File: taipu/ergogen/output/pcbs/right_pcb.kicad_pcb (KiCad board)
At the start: 2 copper layers, 162.9 x 92.4 mm, 0 parts

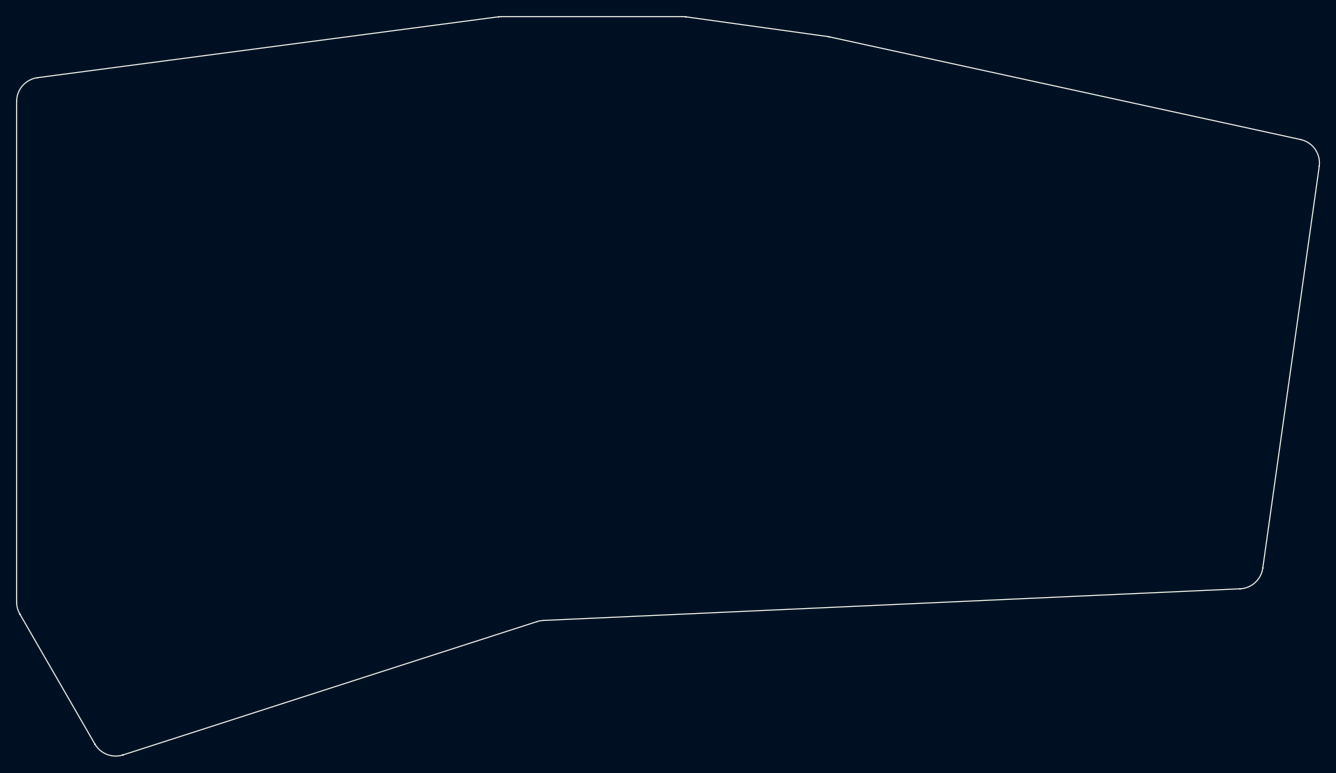
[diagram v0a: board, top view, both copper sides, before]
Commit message: mounting holes and net
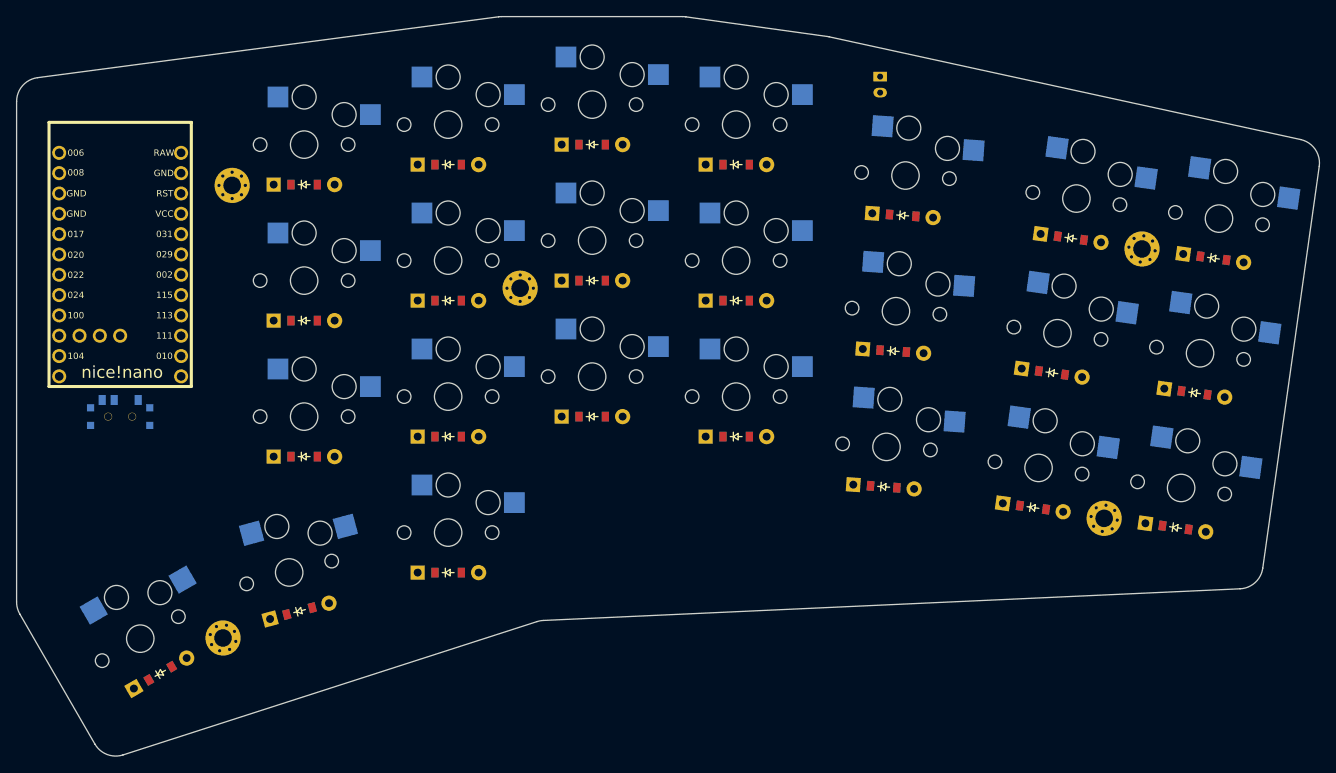
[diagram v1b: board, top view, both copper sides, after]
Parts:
- added D1: , ComboDiode, F.Cu at (376.2, 138.1)
- added D10: , ComboDiode, F.Cu at (321.3, 126.7)
- added D11: , ComboDiode, F.Cu at (321.3, 109.7)
- added D12: , ComboDiode, F.Cu at (321.3, 92.7)
- added D13: , ComboDiode, F.Cu at (303.3, 124.2)
- added D14: , ComboDiode, F.Cu at (303.3, 107.2)
- added D15: , ComboDiode, F.Cu at (303.3, 90.2)
- added D16: , ComboDiode, F.Cu at (285.3, 143.7)
- added D17: , ComboDiode, F.Cu at (285.3, 126.7)
- added D18: , ComboDiode, F.Cu at (285.3, 109.7)
- added D19: , ComboDiode, F.Cu at (285.3, 92.7)
- added D2: , ComboDiode, F.Cu at (378.6, 121.3)
- added D20: , ComboDiode, F.Cu at (267.3, 129.2)
- added D21: , ComboDiode, F.Cu at (267.3, 112.2)
- added D22: , ComboDiode, F.Cu at (267.3, 95.2)
- added D23: , ComboDiode, F.Cu at (266.7, 148.6)
- added D24: , ComboDiode, F.Cu at (249.3, 156.3)
- added D3: , ComboDiode, F.Cu at (380.9, 104.4)
- added D4: , ComboDiode, F.Cu at (358.4, 135.6)
- added D5: , ComboDiode, F.Cu at (360.7, 118.8)
- added D6: , ComboDiode, F.Cu at (363.1, 101.9)
- added D7: , ComboDiode, F.Cu at (339.7, 133.0)
- added D8: , ComboDiode, F.Cu at (340.9, 116.1)
- added D9: , ComboDiode, F.Cu at (342.1, 99.1)
- added JST1: , JST_PH_S2B-PH-K_02x2.00mm_Angled, F.Cu at (339.3, 82.7)
- added MCU1: nice_nano, nice_nano, F.Cu at (244.3, 105.2)
- added S1: , PG1350, F.Cu at (376.9, 133.2)
- added S10: , PG1350, F.Cu at (321.3, 121.7)
- added S11: , PG1350, F.Cu at (321.3, 104.7)
- added S12: , PG1350, F.Cu at (321.3, 87.7)
- added S13: , PG1350, F.Cu at (303.3, 119.2)
- added S14: , PG1350, F.Cu at (303.3, 102.2)
- added S15: , PG1350, F.Cu at (303.3, 85.2)
- added S16: , PG1350, F.Cu at (285.3, 138.7)
- added S17: , PG1350, F.Cu at (285.3, 121.7)
- added S18: , PG1350, F.Cu at (285.3, 104.7)
- added S19: , PG1350, F.Cu at (285.3, 87.7)
- added S2: , PG1350, F.Cu at (379.2, 116.3)
- added S20: , PG1350, F.Cu at (267.3, 124.2)
- added S21: , PG1350, F.Cu at (267.3, 107.2)
- added S22: , PG1350, F.Cu at (267.3, 90.2)
- added S23: , PG1350, F.Cu at (265.4, 143.7)
- added S24: , PG1350, F.Cu at (246.8, 152.0)
- added S3: , PG1350, F.Cu at (381.6, 99.5)
- added S4: , PG1350, F.Cu at (359.1, 130.7)
- added S5: , PG1350, F.Cu at (361.4, 113.8)
- added S6: , PG1350, F.Cu at (363.8, 97.0)
- added S7: , PG1350, F.Cu at (340.1, 128.0)
- added S8: , PG1350, F.Cu at (341.2, 111.1)
- added S9: , PG1350, F.Cu at (342.4, 94.1)
- added T1: , E73:SPDT_C128955, F.Cu at (244.3, 124.2)
- added _1: , MountingHole_2.2mm_M2_Pad_Via, F.Cu at (372.0, 103.3)
- added _2: , MountingHole_2.2mm_M2_Pad_Via, F.Cu at (258.3, 95.3)
- added _3: , MountingHole_2.2mm_M2_Pad_Via, F.Cu at (294.3, 108.2)
- added _4: , MountingHole_2.2mm_M2_Pad_Via, F.Cu at (367.3, 137.0)
- added _5: , MountingHole_2.2mm_M2_Pad_Via, F.Cu at (257.1, 151.9)

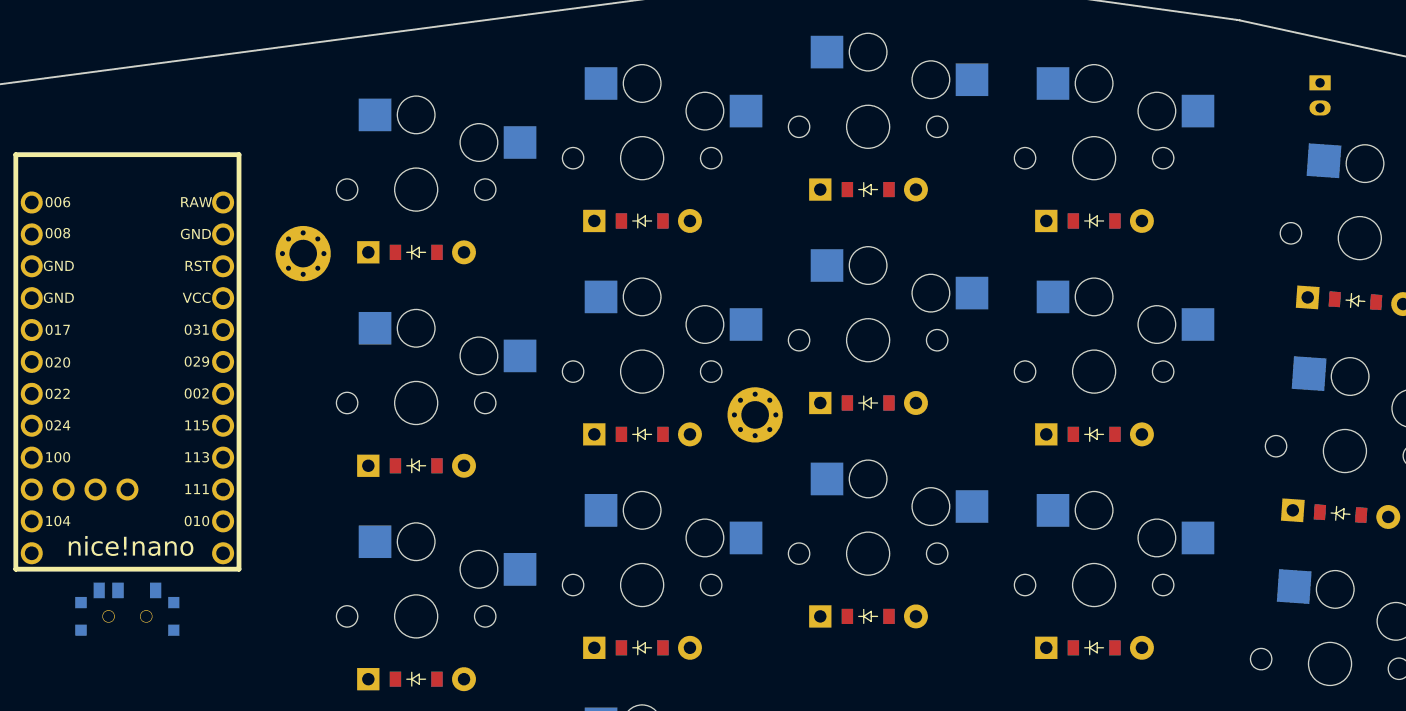
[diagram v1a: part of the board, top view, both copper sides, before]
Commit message: better batery placement
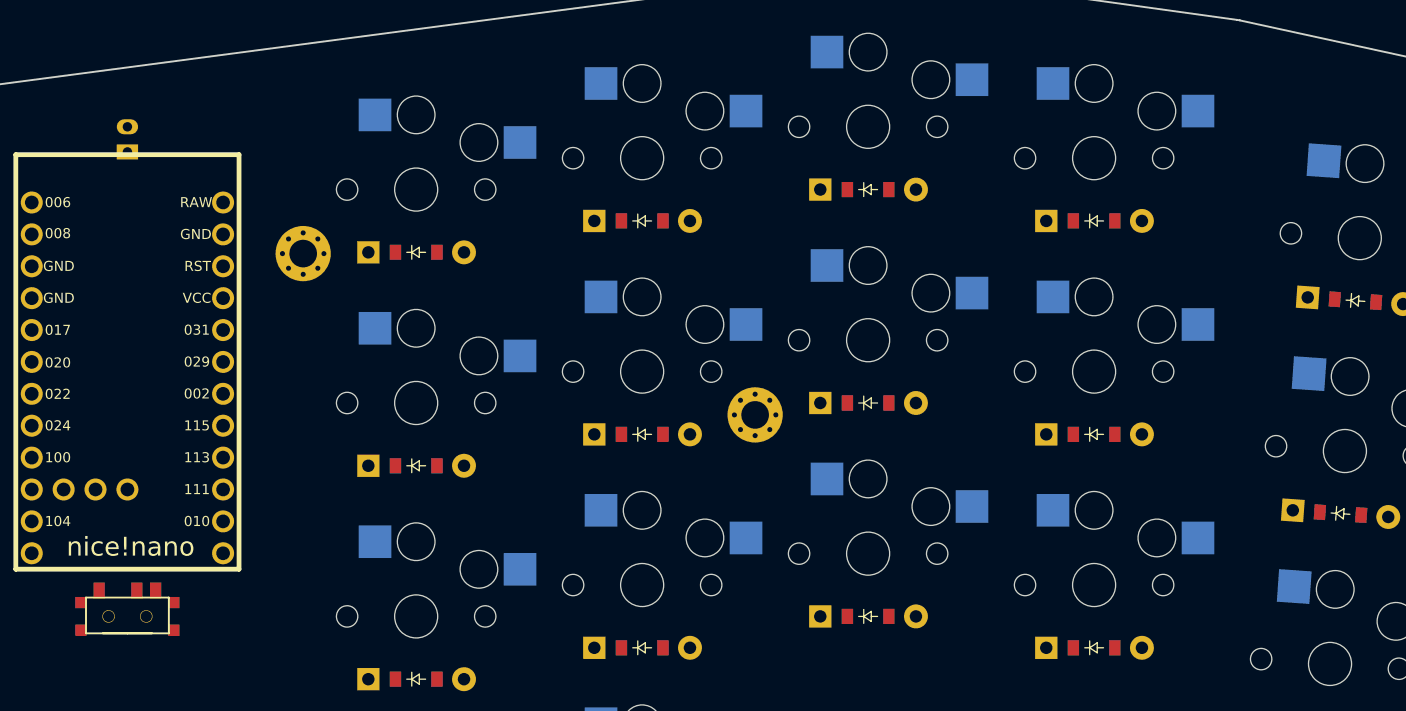
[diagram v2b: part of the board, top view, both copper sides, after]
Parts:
- moved JST1 95.1 mm to (244.3, 86.2), turned to 90 degrees
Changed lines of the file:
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@@
         (descr "JST PH series connector, S2B-PH-K, side entry type, through hole, Datasheet: http://www.jst-mfg.com/product/pdf/eng/ePH.pdf")
         (tags "connector jst ph")
-        (at 339.257021 82.74633159999999 -90)
+        (at 244.257021 86.24633159999999 90)
         (fp_text reference "JST1" (at 0 0) (layer F.SilkS) hide (effects (font (size 1.27 1.27) (thickness 0.15))))
         (fp_text value "" (at 0 0) (layer F.SilkS) hide (effects (font (size 1.27 1.27) (thickness 0.15))))
@@
         (fp_line (start -1 1.5) (end -1 2.0) (layer B.SilkS) (width 0.15))
         (fp_line (start -1.25 1.75) (end -0.75 1.75) (layer B.SilkS) (width 0.15))
-        (pad 1 thru_hole rect (at -1 0 -90) (size 1.2 1.7) (drill 0.75) (layers *.Cu *.Mask) (net 50 "pos"))
-        (pad 2 thru_hole oval (at 1 0 -90) (size 1.2 1.7) (drill 0.75) (layers *.Cu *.Mask) (net 37 "GND"))
+        (pad 1 thru_hole rect (at -1 0 90) (size 1.2 1.7) (drill 0.75) (layers *.Cu *.Mask) (net 50 "pos"))
+        (pad 2 thru_hole oval (at 1 0 90) (size 1.2 1.7) (drill 0.75) (layers *.Cu *.Mask) (net 37 "GND"))
     )
         (module E73:SPDT_C128955 (layer F.Cu)
@@
             (fp_text reference "T1" (at 0 0) (layer F.SilkS) hide (effects (font (size 1.27 1.27) (thickness 0.15))))
             (fp_text value "" (at 0 0) (layer F.SilkS) hide (effects (font (size 1.27 1.27) (thickness 0.15))))
-            (fp_line (start 1.95 -1.35) (end -1.95 -1.35) (layer B.SilkS) (width 0.15))
-            (fp_line (start 0 -1.35) (end -3.3 -1.35) (layer B.SilkS) (width 0.15))
-            (fp_line (start -3.3 -1.35) (end -3.3 1.5) (layer B.SilkS) (width 0.15))
-            (fp_line (start -3.3 1.5) (end 3.3 1.5) (layer B.SilkS) (width 0.15))
-            (fp_line (start 3.3 1.5) (end 3.3 -1.35) (layer B.SilkS) (width 0.15))
-            (fp_line (start 0 -1.35) (end 3.3 -1.35) (layer B.SilkS) (width 0.15))
+            (fp_line (start 1.95 -1.35) (end -1.95 -1.35) (layer F.SilkS) (width 0.15))
+            (fp_line (start 0 -1.35) (end -3.3 -1.35) (layer F.SilkS) (width 0.15))
+            (fp_line (start -3.3 -1.35) (end -3.3 1.5) (layer F.SilkS) (width 0.15))
+            (fp_line (start -3.3 1.5) (end 3.3 1.5) (layer F.SilkS) (width 0.15))
+            (fp_line (start 3.3 1.5) (end 3.3 -1.35) (layer F.SilkS) (width 0.15))
+            (fp_line (start 0 -1.35) (end 3.3 -1.35) (layer F.SilkS) (width 0.15))
             (fp_line (start -1.95 -3.85) (end 1.95 -3.85) (layer Dwgs.User) (width 0.15))
             (fp_line (start 1.95 -3.85) (end 1.95 -1.35) (layer Dwgs.User) (width 0.15))
@@
             (pad "" np_thru_hole circle (at 1.5 0) (size 1 1) (drill 0.9) (layers *.Cu *.Mask))
             (pad "" np_thru_hole circle (at -1.5 0) (size 1 1) (drill 0.9) (layers *.Cu *.Mask))
-            (pad 1 smd rect (at -2.25 2.075 180) (size 0.9 1.25) (layers B.Cu B.Paste B.Mask) (net 50 "pos"))
-            (pad 2 smd rect (at 0.75 2.075 180) (size 0.9 1.25) (layers B.Cu B.Paste B.Mask) (net 36 "RAW"))
-            (pad 3 smd rect (at 2.25 2.075 180) (size 0.9 1.25) (layers B.Cu B.Paste B.Mask))
-            (pad "" smd rect (at 3.7 -1.1 180) (size 0.9 0.9) (layers B.Cu B.Paste B.Mask))
-            (pad "" smd rect (at 3.7 1.1 180) (size 0.9 0.9) (layers B.Cu B.Paste B.Mask))
-            (pad "" smd rect (at -3.7 1.1 180) (size 0.9 0.9) (layers B.Cu B.Paste B.Mask))
-            (pad "" smd rect (at -3.7 -1.1 180) (size 0.9 0.9) (layers B.Cu B.Paste B.Mask))
+            (pad 1 smd rect (at 2.25 2.075 180) (size 0.9 1.25) (layers F.Cu F.Paste F.Mask) (net 50 "pos"))
+            (pad 2 smd rect (at -0.75 2.075 180) (size 0.9 1.25) (layers F.Cu F.Paste F.Mask) (net 36 "RAW"))
+            (pad 3 smd rect (at -2.25 2.075 180) (size 0.9 1.25) (layers F.Cu F.Paste F.Mask))
+            (pad "" smd rect (at 3.7 -1.1 180) (size 0.9 0.9) (layers F.Cu F.Paste F.Mask))
+            (pad "" smd rect (at 3.7 1.1 180) (size 0.9 0.9) (layers F.Cu F.Paste F.Mask))
+            (pad "" smd rect (at -3.7 1.1 180) (size 0.9 0.9) (layers F.Cu F.Paste F.Mask))
+            (pad "" smd rect (at -3.7 -1.1 180) (size 0.9 0.9) (layers F.Cu F.Paste F.Mask))
         )
     (module "MountingHole_2.2mm_M2_Pad_Via" (version 20210722) (generator pcbnew) (layer "F.Cu")
